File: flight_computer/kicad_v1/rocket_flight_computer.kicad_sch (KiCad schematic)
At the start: 8 parts, among them U2 Teensy4.1, U3 BMI088, U5 BMP280

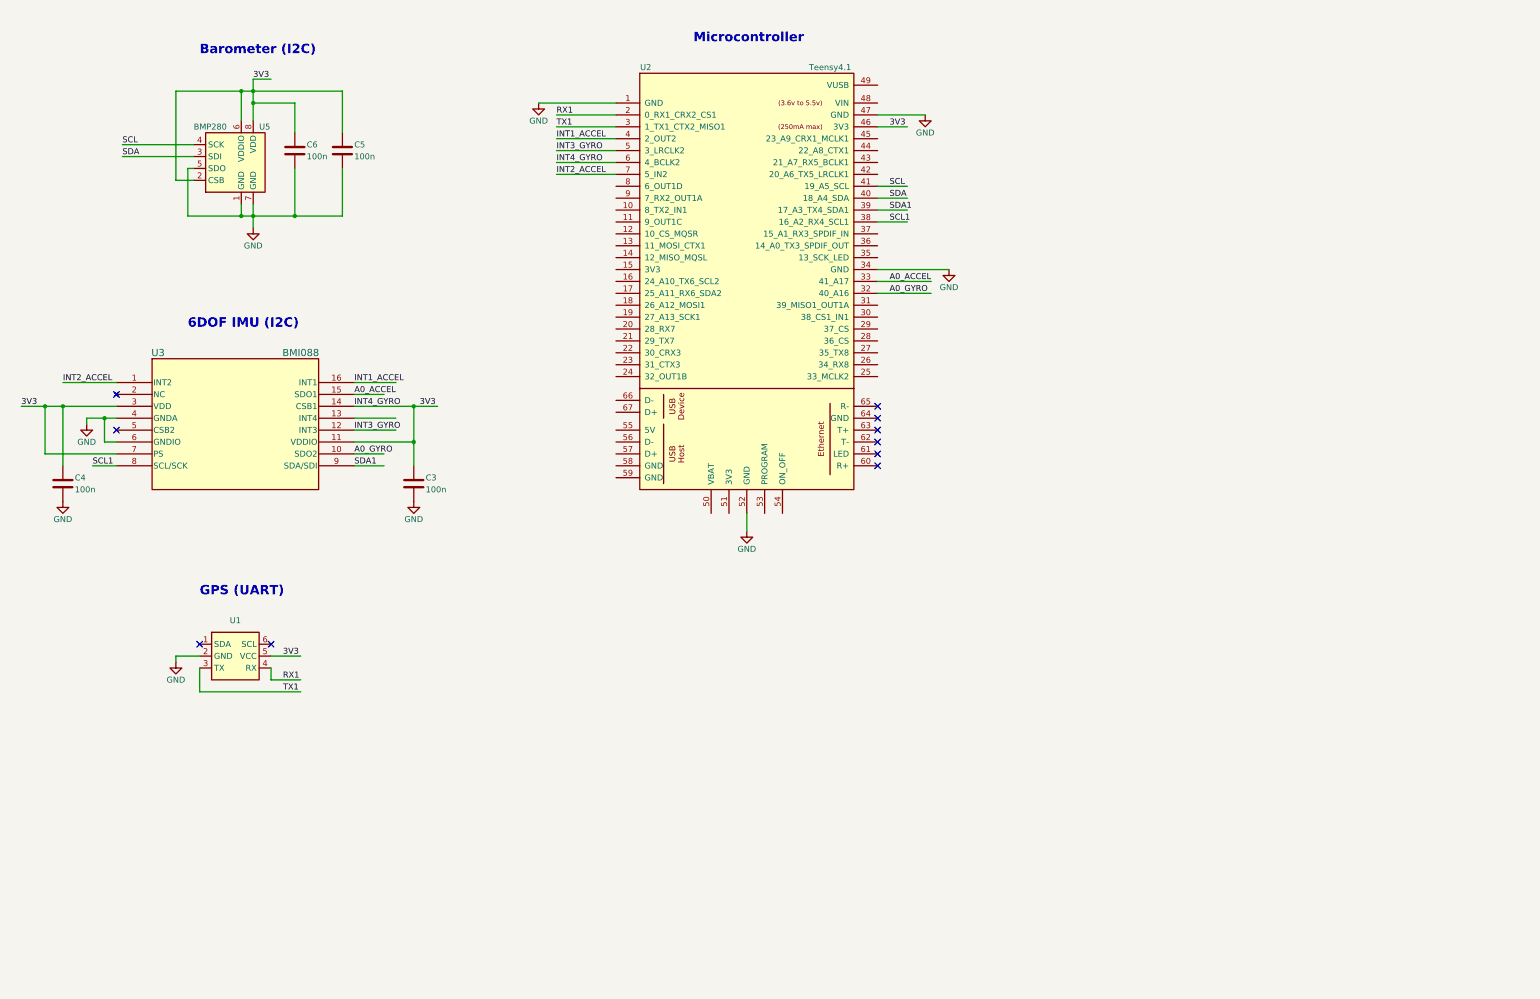
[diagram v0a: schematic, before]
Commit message: add segment display to symbols lib and to schematic
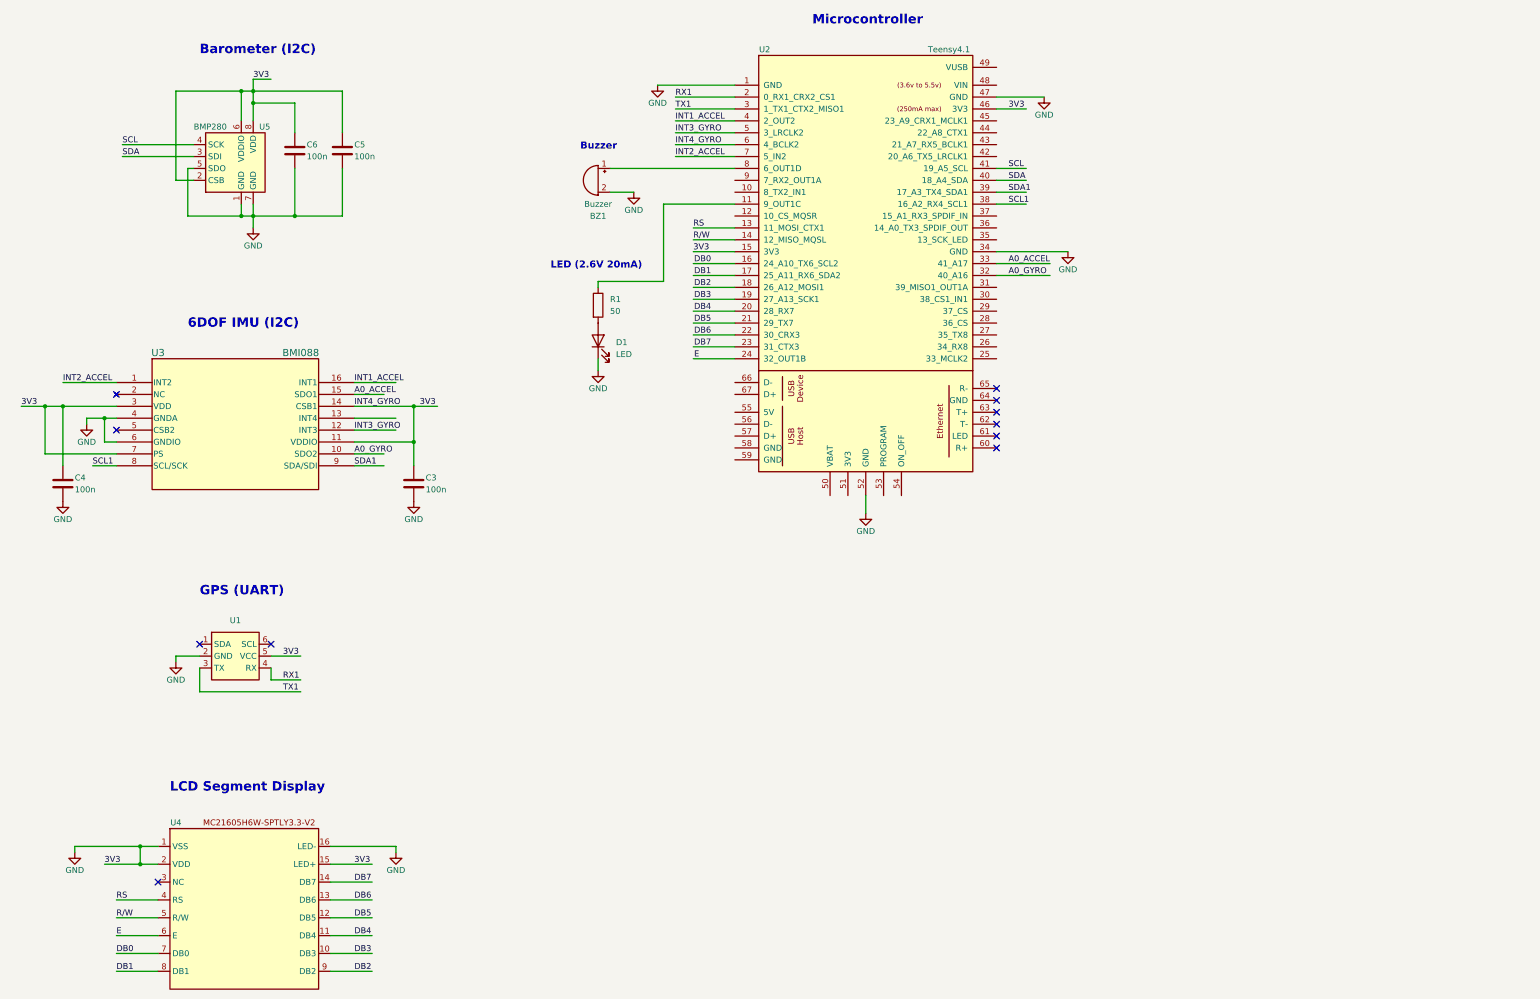
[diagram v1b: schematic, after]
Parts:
- added BZ1: Buzzer, symbol Device:Buzzer
- added D1: LED, symbol Device:LED
- added R1: 50, symbol Device:R
- added U4: ~, symbol components:MC21605H6W-SPTLY3.3-V2
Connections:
- net 3V3 is gone; now on net GND: C3.1, C4.1, C5.1, C6.1, U1.5 (VCC), U2.46 (3V3), U2.6 (4_BCLK2), U3.11 (VDDIO), U3.14 (CSB1), U3.3 (VDD), U3.7 (PS), U5.2 (CSB), U5.6 (VDDIO), U5.8 (VDD)
- net GND: now also U2.15 (3V3), BZ1.2 (+), D1.1 (K), U4.1 (VSS), U4.15 (LED+), U4.16 (LED-), U4.2 (VDD)
- net at U2.11 (9_OUT1C): now also R1.1
- net RS: now reaches U2.13 (11_MOSI_CTX1)
- net RS: now also U4.4 (RS)
- net R/W: now reaches U2.14 (12_MISO_MQSL)
- net R/W: now also U4.5 (R/W)
- net DB0: now reaches U2.16 (24_A10_TX6_SCL2)
- net DB0: now also U4.7 (DB0)
- net DB1: now reaches U2.17 (25_A11_RX6_SDA2)
- net DB1: now also U4.8 (DB1)
- net DB2: now reaches U2.18 (26_A12_MOSI1)
- net DB2: now also U4.9 (DB2)
- net DB3: now reaches U2.19 (27_A13_SCK1)
- net DB3: now also U4.10 (DB3)
- net DB4: now reaches U2.20 (28_RX7)
- net DB4: now also U4.11 (DB4)
- net DB5: now reaches U2.21 (29_TX7)
- net DB5: now also U4.12 (DB5)
- net DB6: now reaches U2.22 (30_CRX3)
- net DB6: now also U4.13 (DB6)
- net DB7: now reaches U2.23 (31_CTX3)
- net DB7: now also U4.14 (DB7)
- net E: now reaches U2.24 (32_OUT1B)
- net E: now also U4.6 (E)
- net at U2.8 (6_OUT1D): now also BZ1.1 (-)
- new net: D1.2 (A), R1.2
- no-connect marks 10 -> 11
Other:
- note added: "Buzzer"
- note added: "LCD Segment Display"
- note added: "LED (2.6V 20mA)"
- moved on the sheet: U2

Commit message: start airbrake model in c and add RF module to schematic
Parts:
- added U6: ~, symbol components:XBEE_TH
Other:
- note added: "RF Module (Transmitter)"
- company: (none) -> UCL Rocket
- title: (none) -> Flight Computer
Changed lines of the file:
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@@
 (kicad_sch (version 20230121) (generator eeschema)
   (paper "A3")
+  (title_block
+    (title "Flight Computer")
+    (company "UCL Rocket")
+  )
   (junction (at 38.1 120.65) (diameter 0) (color 0 0 0 0)
   )
@@
   (wire (pts (xy 181.61 77.47) (xy 166.37 77.47))
     (stroke (width 0) (type default))
+  )
+  (text "RF Module (Transmitter)" (at 293.37 43.18 0)
+    (effects (font (size 2 2) (thickness 0.4) bold) (justify left bottom))
   )
   (text "Buzzer" (at 148.59 66.04 0)
@@
         (path "/e4d552e0-a19a-4fc3-a9c2-1c96e50d3231"
           (reference "#PWR02") (unit 1)
+        )
+      )
+    )
+  )
+  (symbol (lib_id "components:XBEE_TH") (at 313.69 73.66 0) (unit 1)
+    (in_bom yes) (on_board yes) (dnp no)
+    (property "Reference" "U6" (at 334.01 53.34 0)
+      (effects (font (size 1.27 1.27)))
+    )
+    (property "Value" "~" (at 334.01 53.34 0)
+      (effects (font (size 1.27 1.27)))
+    )
+    (property "Footprint" "" (at 334.01 53.34 0)
+      (effects (font (size 1.27 1.27)) hide)
+    )
+    (property "Datasheet" "" (at 334.01 53.34 0)
+      (effects (font (size 1.27 1.27)) hide)
+    )
+    (pin "4")
+    (pin "19")
+    (pin "18")
+    (pin "20")
+    (pin "2")
+    (pin "3")
+    (pin "16")
+    (pin "14")
+    (pin "9")
+    (pin "1")
+    (pin "10")
+    (pin "12")
+    (pin "11")
+    (pin "8")
+    (pin "13")
+    (pin "5")
+    (pin "7")
+    (pin "6")
+    (pin "17")
+    (pin "15")
+    (instances
+      (project "rocket_flight_computer"
+        (path "/e4d552e0-a19a-4fc3-a9c2-1c96e50d3231"
+          (reference "U6") (unit 1)
         )
       )
@@
   )
   (symbol (lib_id "components:BN-880") (at 74.93 173.99 0) (unit 1)
-    (in_bom yes) (on_board yes) (dnp no) (fields_autoplaced)
-    (property "Reference" "U1" (at 74.93 166.37 0)
-      (effects (font (size 1.27 1.27)))
-    )
+    (in_bom yes) (on_board yes) (dnp no)
+    (property "Reference" "U1" (at 71.12 167.64 0)
+      (effects (font (size 1.27 1.27)))
+    )

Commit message: add motor behavior to model
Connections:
- net GND: now also U6.1 (VCC), U6.10 (GND)
- net RS: now also U2.43 (21_A7_RX5_BCLK1); no longer U2.13 (11_MOSI_CTX1)
- net R/W: now also U2.42 (20_A6_TX5_LRCLK1); no longer U2.14 (12_MISO_MQSL)
- net MOSI: now reaches U6.11 (DI04/SPI_MOSI)
- net MOSI: now also U2.13 (11_MOSI_CTX1)
- net CS: now reaches U6.17 (DI03/AD3/SPI_~{SSEL})
- net CS: now also U2.12 (10_CS_MQSR)
- net SCK: now reaches U6.18 (DIO2/AD2/SPI__CLK)
- net SCK: now also U2.35 (13_SCK_LED)
- net ATTN: now reaches U6.19 (DIO1/AD1/SPI_~{ATTN})
- net ATTN: now also U2.36 (14_A0_TX3_SPDIF_OUT)
- net MISO: now reaches U6.4 (SPI_MISO)
- net MISO: now also U2.14 (12_MISO_MQSL)
- net RST: now reaches U6.5 (~{RESET})
- net RST: now also U2.37 (15_A1_RX3_SPDIF_IN)
- no-connect marks 11 -> 23
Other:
- note added: "RF Module (Transmitter) (SPI)"
- note removed: "RF Module (Transmitter)"
- moved on the sheet: U1, U4

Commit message: noise filterring control and SSR in schematic
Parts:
- added R2, R3: 400, symbol Device:R
- added U7, U8: ~, symbol components:G3VM_Relay
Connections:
- net GND: now also U7.2, U8.2
- net I_F1: now reaches U2.26 (34_RX8)
- net I_F1: now also R2.1
- net I_F2: now reaches U2.27 (35_TX8)
- net I_F2: now also R3.1
- new net: R3.2, U8.1
- new net: R2.2, U7.1
- new net 12V_IN: U7.4, U8.4
- new net 12V_OUT1: U7.3
- new net 12V_OUT2: U8.3
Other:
- note added: "PYRO CHANNELS (SOLID STATE RELAYS)"

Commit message: noisy c model
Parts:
- added F1, F2, F3, F4, F5, F6, F7, F8: Fuse, symbol Device:Fuse
- renumbered C6 to C1, C5 to C2, C4 to C3, C3 to C4, U5 to U1, U6 to U2, U2 to U3, U3 to U4, U7 to U5, U8 to U6, U1 to U7, U4 to U8
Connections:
- net GND: now also F7.2; no longer C1.1, C2.1, C3.1, C4.1, U1.2 (CSB), U1.6 (VDDIO), U1.8 (VDD), U2.1 (VCC), U3.15 (3V3), U3.46 (3V3), U3.6 (4_BCLK2), U4.11 (VDDIO), U4.14 (CSB1), U4.3 (VDD), U4.7 (PS), U7.5 (VCC), U8.15 (LED+)
- net at U3.48 (VIN): now also F2.1
- new net: C3.1, F4.2, U4.3 (VDD), U4.7 (PS)
- new net: C1.1, C2.1, F1.1, U1.2 (CSB), U1.6 (VDDIO), U1.8 (VDD)
- new net: F3.2, U2.1 (VCC)
- new net: F8.1, U8.15 (LED+)
- new net: F6.1, U7.5 (VCC)
- new net 3V3: F1.2, F3.1, F4.1, F5.2, F6.2, F7.1, F8.2, U3.15 (3V3), U3.46 (3V3)
- new net INT4_GYRO: C4.1, F5.1, U3.6 (4_BCLK2), U4.11 (VDDIO), U4.14 (CSB1)
- new net VIN: F2.2
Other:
- note added: "LED (ADAPT*)"
- note added: "SOLID STATE RELAYS"
- note removed: "LED (2.6V 20mA)"
- note removed: "PYRO CHANNELS (SOLID STATE RELAYS)"
- moved on the sheet: BZ1, C3, C4, D1, R1, R2, R3, U2, U3, U4, U5, U6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
